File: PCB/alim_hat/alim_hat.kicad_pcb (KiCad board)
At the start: 2 copper layers, 85 x 56 mm, 41 parts, among them J1 Screw_Terminal_01x04, J10 Conn_01x02, J11 Conn_01x02, J12 Conn_01x02, J2 Jack-DC, J3 Conn_02x04_Odd_Even, J4 Jack-DC, J5 Jack-DC, J6 Jack-DC, J7 Jack-DC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

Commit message: complet new polarity protection
update fab file
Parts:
- added C1: 100uF, capa:CAPAE660X800N, F.Cu at (221.4, 133.5)
- added D1: MM1Z15, Diode_SMD:D_SOD-123, F.Cu at (224.7, 144.5)
- added R14: 470k, Resistor_SMD:R_0805_2012Metric, F.Cu at (228.9, 147.2)
- F2, F3, F4, F5: value Polyfuse_Small -> 2920L330/24
- J2: value Jack-DC -> XT30
- MK1, MK2, MK3, MK4: value M2.5 -> M3
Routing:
- net Net-(D1-Pad1): track 7.20 -> 11.5 mm

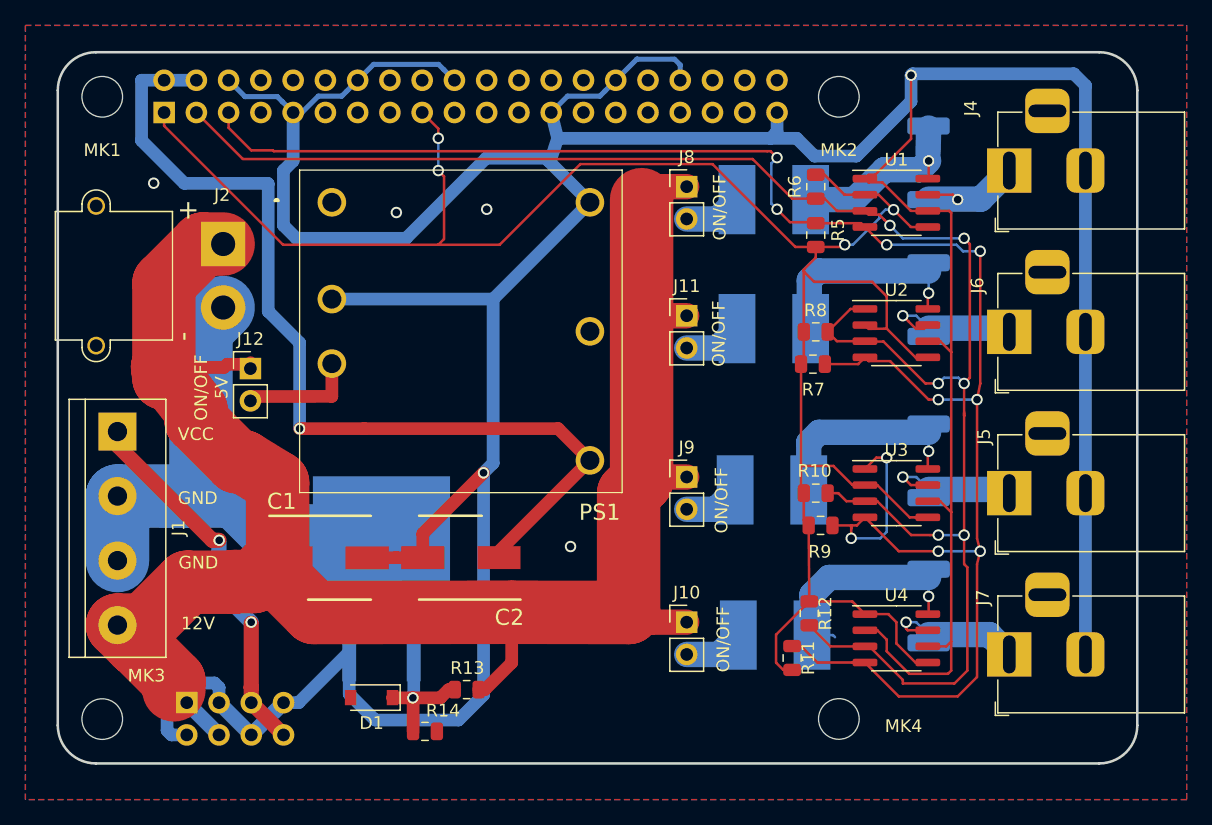
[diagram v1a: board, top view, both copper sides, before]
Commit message: update alim and relais pcb 2-> 4 couches
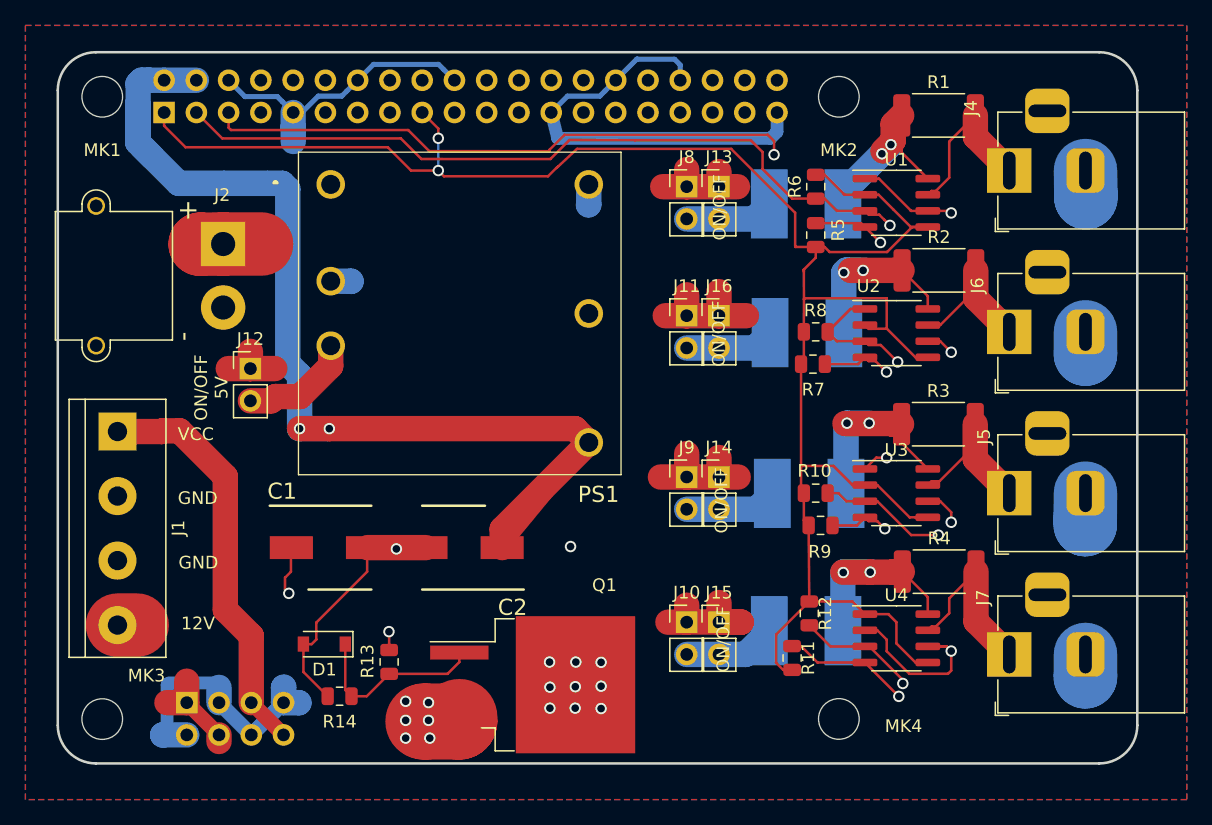
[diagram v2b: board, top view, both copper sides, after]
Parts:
- added J13: Conn_01x02, Connector_PinHeader_2.54mm:PinHeader_1x02_P2.54mm_Vertical, F.Cu at (252.1, 104.3)
- added J14: Conn_01x02, Connector_PinHeader_2.54mm:PinHeader_1x02_P2.54mm_Vertical, F.Cu at (252.1, 127.1)
- added J15: Conn_01x02, Connector_PinHeader_2.54mm:PinHeader_1x02_P2.54mm_Vertical, F.Cu at (252.1, 138.6)
- added J16: Conn_01x02, Connector_PinHeader_2.54mm:PinHeader_1x02_P2.54mm_Vertical, F.Cu at (252.1, 114.4)
- Q1, R1, R2, R3, R4: moved to F.Cu
- moved Q1 14.5 mm to (237.4, 143.5), turned to 0 degrees
- moved R14 7.27 mm to (222.2, 144.4), turned to 180 degrees
- moved R13 6.49 mm to (226.1, 141.7), turned to 270 degrees
- moved D1 5.61 mm to (221.0, 140.3)
- moved R1 3.82 mm to (269.4, 98.7), turned to 0 degrees
- moved R3 2.99 mm to (269.4, 123.0), turned to 0 degrees
- moved F4 2.94 mm to (259.2, 128.4)
- moved R4 2.83 mm to (269.4, 134.6), turned to 0 degrees
- moved F3 2.63 mm to (259.0, 115.8)
- moved F2 2.56 mm to (258.9, 105.6)
- moved F5 2.46 mm to (258.9, 139.2)
- moved R2 2.44 mm to (269.4, 110.9), turned to 0 degrees
- moved PS1 1.41 mm to (221.5, 104.1)
- moved C2 0.83 mm to (232.0, 132.7)
- moved C1 0.80 mm to (221.4, 132.7)
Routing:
- net GND: track 348.5 -> 165.3 mm, vias 6 -> 12
- net +12V: track 244.7 -> 62.1 mm, vias 0 -> 2
- net /gnd_no: track 47.0 -> 10.1 mm, vias 0 -> 9
- net /SCL: track 156.4 -> 123.0 mm, vias 10 -> 6
- net +5V: track 75.3 -> 94.0 mm, vias 1 -> 2
- net /SDA: track 142.6 -> 129.3 mm, vias 6 -> 4
- net +3V3: track 166.9 -> 160.2 mm, vias 4 -> 2
- net VCC: track 35.7 -> 32.3 mm, vias 2 -> 0
- net Net-(J7-Pad1): track 11.5 -> 14.8 mm, vias 1 -> 0
- net Net-(D1-Pad1): track 11.5 -> 14.7 mm, vias 1 -> 0
- net Net-(F5-Pad1): track 4.70 -> 7.27 mm
- net Net-(F4-Pad1): track 4.44 -> 7.00 mm
- net Net-(J5-Pad1): track 11.1 -> 13.7 mm, vias 1 -> 0
- net Net-(F3-Pad1): track 4.59 -> 6.97 mm
- net Net-(F2-Pad1): track 4.59 -> 6.89 mm
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- added copper zone on F.Cu, net +12V
- added copper zone on In2.Cu, net /gnd_no
- added copper zone on In1.Cu, net GND
- removed copper zone on F.Cu, net GND
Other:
- copper layers 2 -> 4
